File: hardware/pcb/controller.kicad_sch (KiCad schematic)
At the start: 23 parts, among them J2 Conn_02x13_Odd_Even, J3 JTAG 1,27mm, U3 ESP32-WROOM-32E, U5 CP2102N-Axx-xQFN28

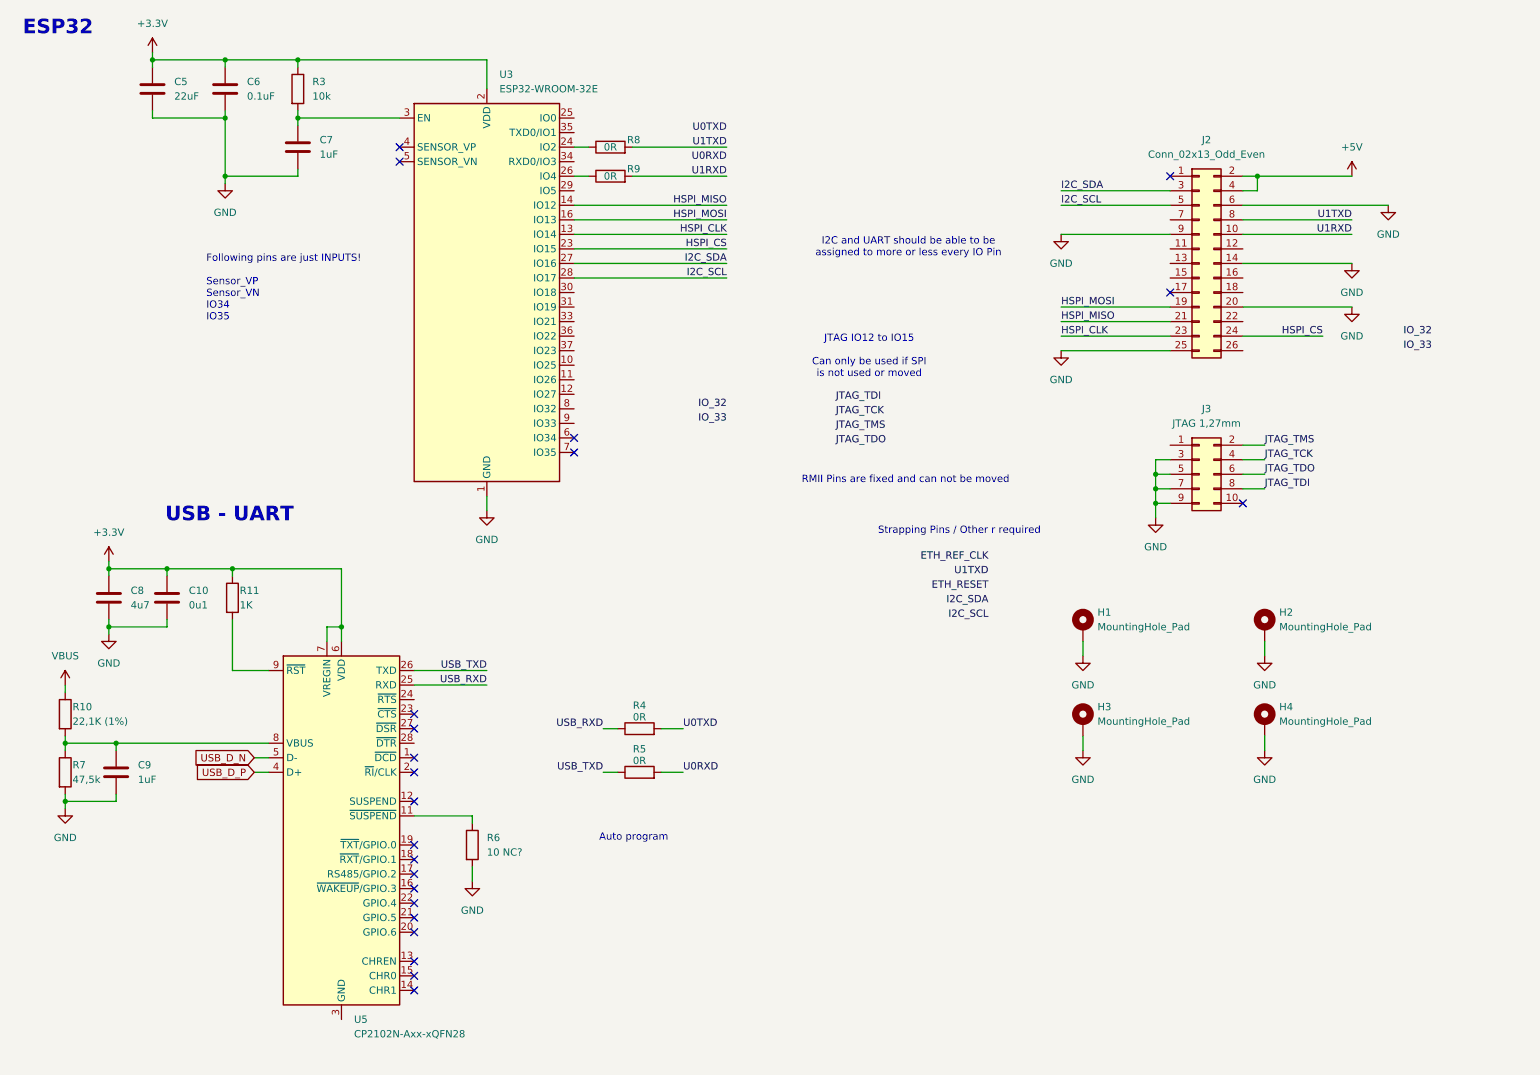
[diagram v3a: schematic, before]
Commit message: draft: Added pin connections to esp32
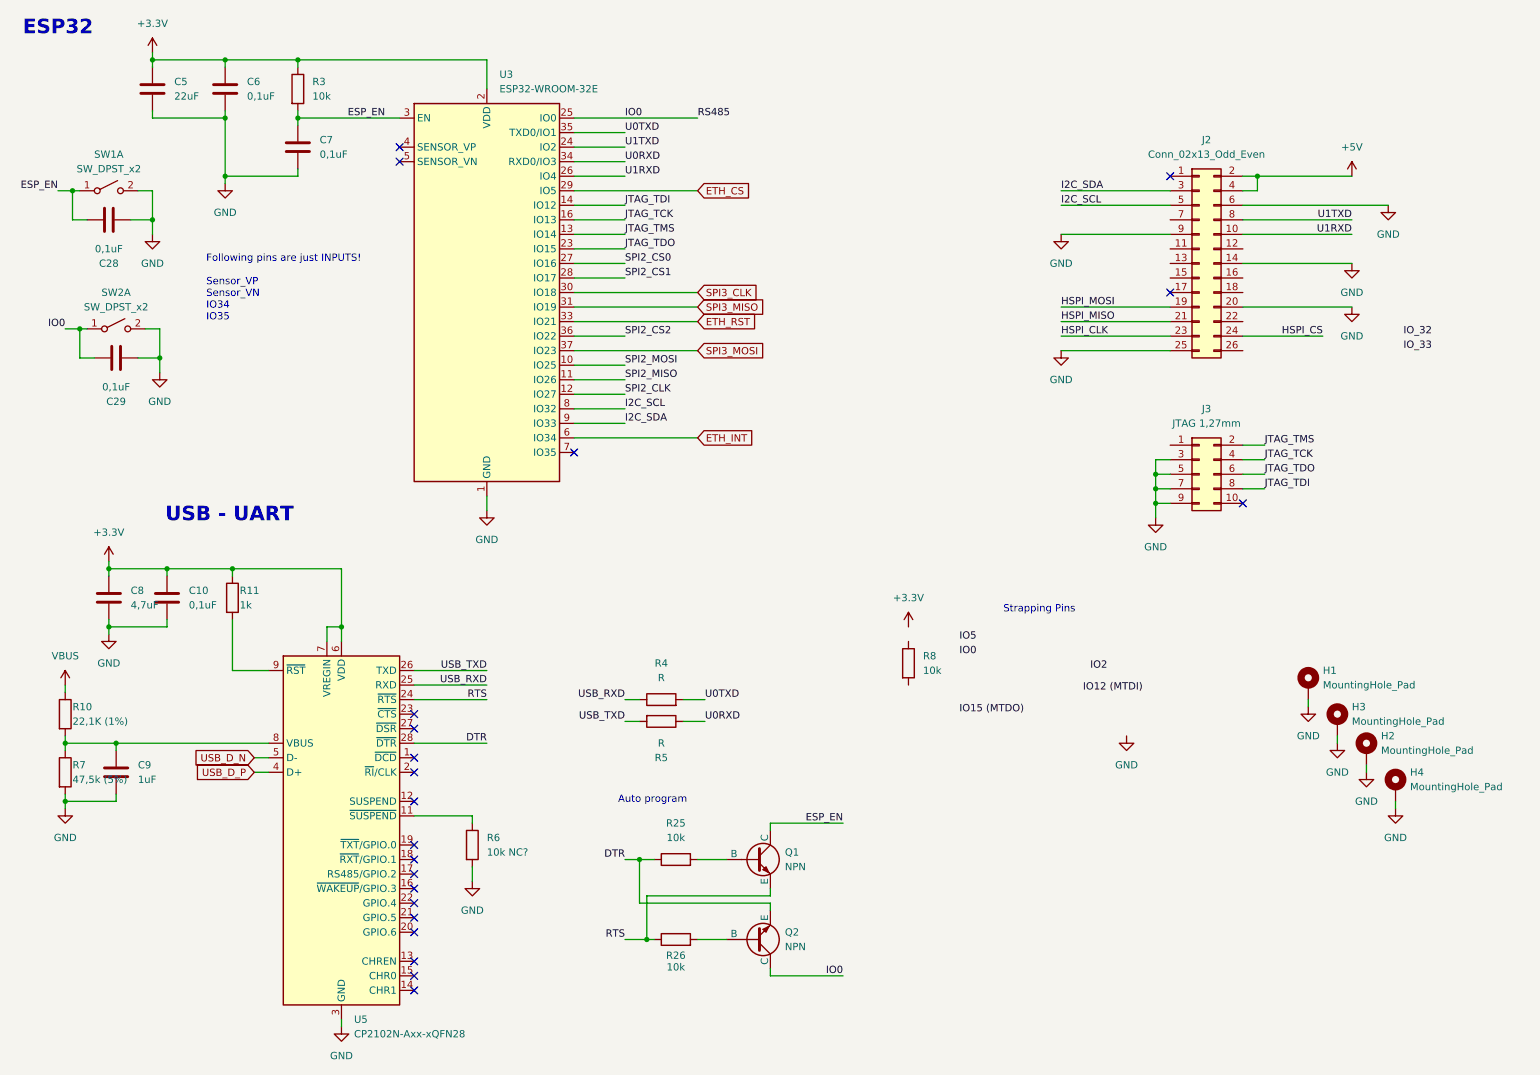
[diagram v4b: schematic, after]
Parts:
- removed R9: 0R, symbol Device:R
- added C28, C29: 0,1uF, symbol Device:C
- added Q1, Q2: NPN, symbol Simulation_SPICE:NPN
- added R25, R26: 10k, symbol Device:R
- added SW1, SW2: SW_DPST_x2, symbol Switch:SW_DPST_x2
- C10: value 0u1 -> 0,1uF
- C6: value 0.1uF -> 0,1uF
- C7: value 1uF -> 0,1uF
- C8: value 4u7 -> 4,7uF
- R11: value 1K -> 1k
- R4, R5: value 0R -> R
- R6: value 10 NC? -> 10k NC?
- R7: value 47,5k -> 47,5k (5%)
- R8: value 0R -> 10k
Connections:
- net GND: now also U5.29 (GND), U5.3 (GND), C28.1, C29.1, SW1.2 (B), SW2.2 (B)
- net HSPI_CLK: no longer U3.13 (IO14)
- net HSPI_CS: no longer U3.23 (IO15)
- net HSPI_MISO: no longer U3.14 (IO12)
- net HSPI_MOSI: no longer U3.16 (IO13)
- net I2C_SCL: now also U3.8 (IO32); no longer U3.28 (IO17)
- net I2C_SDA: now also U3.9 (IO33); no longer U3.27 (IO16)
- net JTAG_TCK: now also U3.16 (IO13)
- net JTAG_TDI: now also U3.14 (IO12)
- net JTAG_TDO: now also U3.23 (IO15)
- net JTAG_TMS: now also U3.13 (IO14)
- net U0RXD: now also R5.1, U3.34 (RXD0/IO3); no longer R5.2
- net U0TXD: now also U3.35 (TXD0/IO1)
- net U1RXD: now also U3.26 (IO4)
- net U1TXD: now also U3.24 (IO2); no longer R8.2
- net USB_TXD: now also R5.2; no longer R5.1
- net at R8.1: no longer U3.24 (IO2)
- net ESP_EN: now reaches C7.1, R3.2, U3.3 (EN)
- net ESP_EN: now also C28.2, Q1.1 (C), SW1.1 (A)
- net SPI2_MOSI: now reaches U3.10 (IO25)
- net SPI2_MISO: now reaches U3.11 (IO26)
- net SPI2_CLK: now reaches U3.12 (IO27)
- net IO0: now reaches U3.25 (IO0)
- net IO0: now also C29.2, Q2.1 (C), SW2.1 (A)
- net ETH_CS: now reaches U3.29 (IO5)
- net SPI3_CLK: now reaches U3.30 (IO18)
- net SPI3_MISO: now reaches U3.31 (IO19)
- net ETH_RST: now reaches U3.33 (IO21)
- net SPI2_CS2: now reaches U3.36 (IO22)
- net SPI3_MOSI: now reaches U3.37 (IO23)
- net ETH_INT: now reaches U3.6 (IO34)
- net RTS: now reaches U5.24 (~{RTS})
- net RTS: now also Q1.3 (E), R26.1
- net DTR: now reaches U5.28 (~{DTR})
- net DTR: now also Q2.3 (E), R25.1
- new net: Q2.2 (B), R26.2
- new net: Q1.2 (B), R25.2
- new net SPI2_CS0: U3.27 (IO16)
- new net SPI2_CS1: U3.28 (IO17)
- no-connect marks 22 -> 21
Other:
- note added: "Strapping Pins"
- note removed: "I2C and UART should be able to be assigned to more or less every IO Pin"
- note removed: "JTAG IO12 to IO15 Can only be used if SPI is not used or moved"
- note removed: "RMII Pins are fixed and can not be moved"
- note removed: "Strapping Pins / Other r required"
- moved on the sheet: H1, H2, H3, H4
